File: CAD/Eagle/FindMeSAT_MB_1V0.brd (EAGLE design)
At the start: 99 x 49.2 mm, 127 parts, among them J291 MCX-J-P-X-RA-SM1, J685 SMA_CON, J701 MOLEX_105017-0001, J801 MICROSIM-8P_SDCARD-8P_MOLEX-1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, J901 JST_S3B-XH-A, Q101 ABS07, Q651 ABM3B-16MHZ-10-R50-1-U, U1001 CFPT-141, U101 ATXMEGA256A3BU-AU, U1011 OPA354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

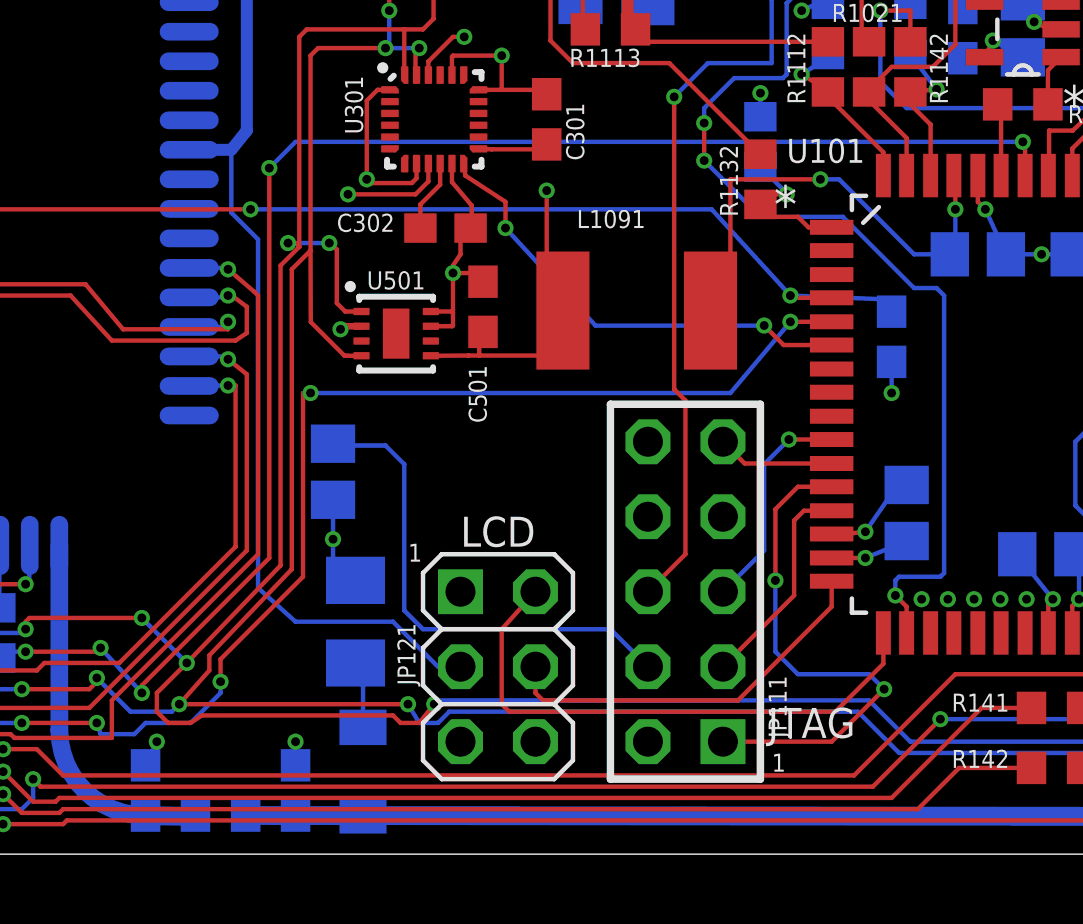
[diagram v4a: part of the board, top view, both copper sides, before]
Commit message: Eagle - I/O header added
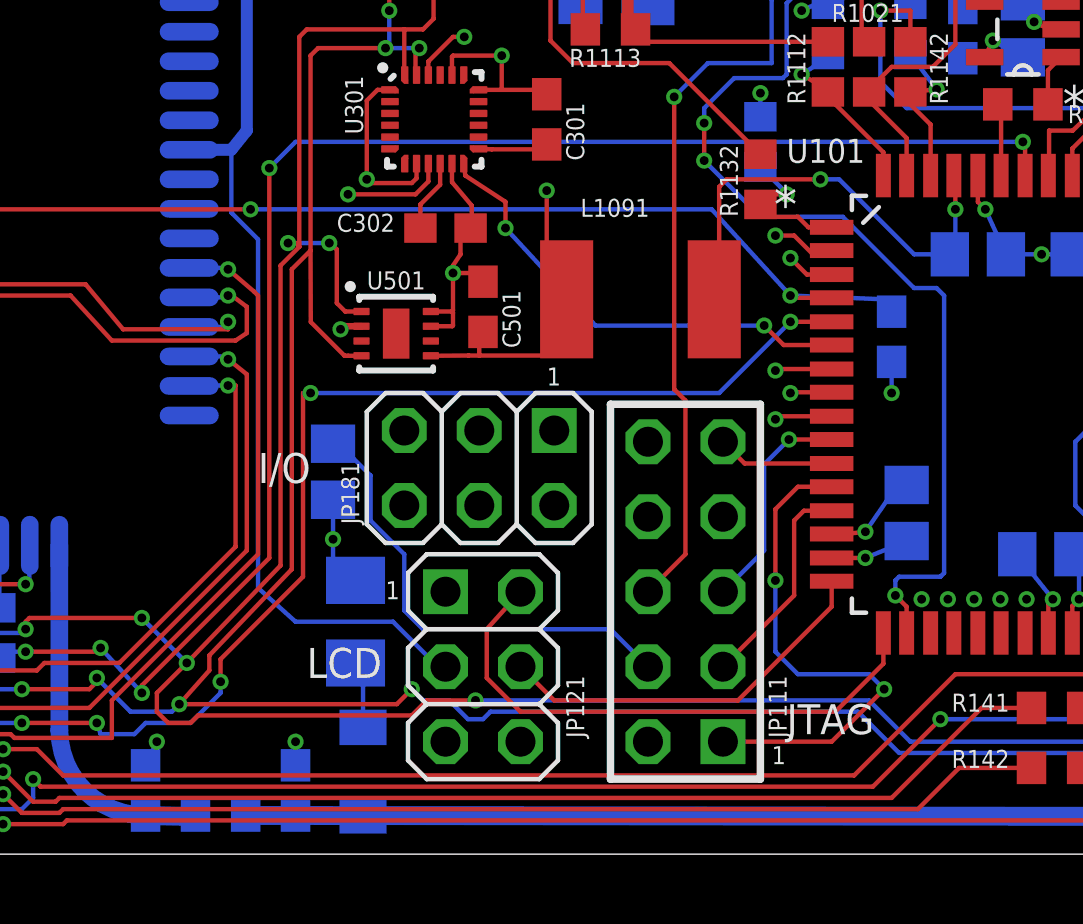
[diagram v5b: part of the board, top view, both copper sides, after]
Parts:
- added JP181: (no value), df4iah_connector:2X03
- moved JP121 0.51 mm to (51.6, 6.35)
- moved L1091 0.40 mm to (56.9, 18.8)
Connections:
- new net IO_AD1: JP181.3, U101.2
- new net IO_AD2: JP181.5, U101.3
- new net IO_D1: JP181.2, U101.7
- new net IO_D2: JP181.4, U101.8
- new net IO_D3: JP181.6, U101.9
- net GND: now also JP181.1
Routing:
- net IO_AD1: track 0.00 -> 25.2 mm, vias 0 -> 1
- net IO_D3: track 0.00 -> 19.1 mm, vias 0 -> 1
- net IO_AD2: track 0.00 -> 17.9 mm, vias 0 -> 1
- net IO_D2: track 0.00 -> 16.3 mm, vias 0 -> 1
- net IO_D1: track 0.00 -> 12.8 mm, vias 0 -> 1
- net VREF: track 16.7 -> 15.8 mm
- net +5V: track 129.0 -> 128.5 mm
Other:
- board text added: "I/O"

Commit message: Eagle - library entries corrected
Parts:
- C1001, C1002, C101, C1012, C1091, C1092, C1093, C1094, C1095, C1096, C1112, C1121, C301, C302, C401, C501, C601, C611, C612, C711: value 100n -> 100nF
- C1011, C141, C201, C251: value 100p -> 100pF
- C1111, C1113, C712: value 47u -> 47uF
- C681: value 68p -> 68pF
- C686: value 18p -> 18pF
- C701: value 1n -> 1nF
- C901: value 100u -> 100uF
- Q101: value ABS07 -> ABS07-32.768KHZ
- R1001, R1011, R1113: value 100k -> 100kR
- R1002, R112: value 10k -> 10kR
- R1012: value 470k -> 470kR
- R1013: value 10 -> 10R
- R1021, R131, R132, R141, R142, R151, R152, R162, R163, R171, R172, R173, R221, R222, R223, R224, R231, R232, R233, R234, R241, R251: value 27 -> 27R
- R111: value 150 -> 150R
- R1111, R1131, R1141: value 4.02k -> 4.02kR
- R1112, R1132: value 6.04k -> 6.04kR
- R1114: value 15k -> 15kR
- R1115: value 68k -> 68kR
- R1142: value 2.0k -> 2.0kR
- R161: value 4.7k -> 4.7kR
- R211, R212: value 3.3k -> 3.3kR
- R701: value 330k -> 330kR
- R721: value 1k5 -> 1.5kR
- R722, R723, R725: value 68 -> 68R
- R724: value 1M -> 1MR
- RPOLY291: value 150mA -> 0A150
- RPOLY711: value 1A -> 1A0
- U1001: value CFPT-141 -> CFPT-141-20MHZ
- U301: value 9DoF IMU -> MPU-9250

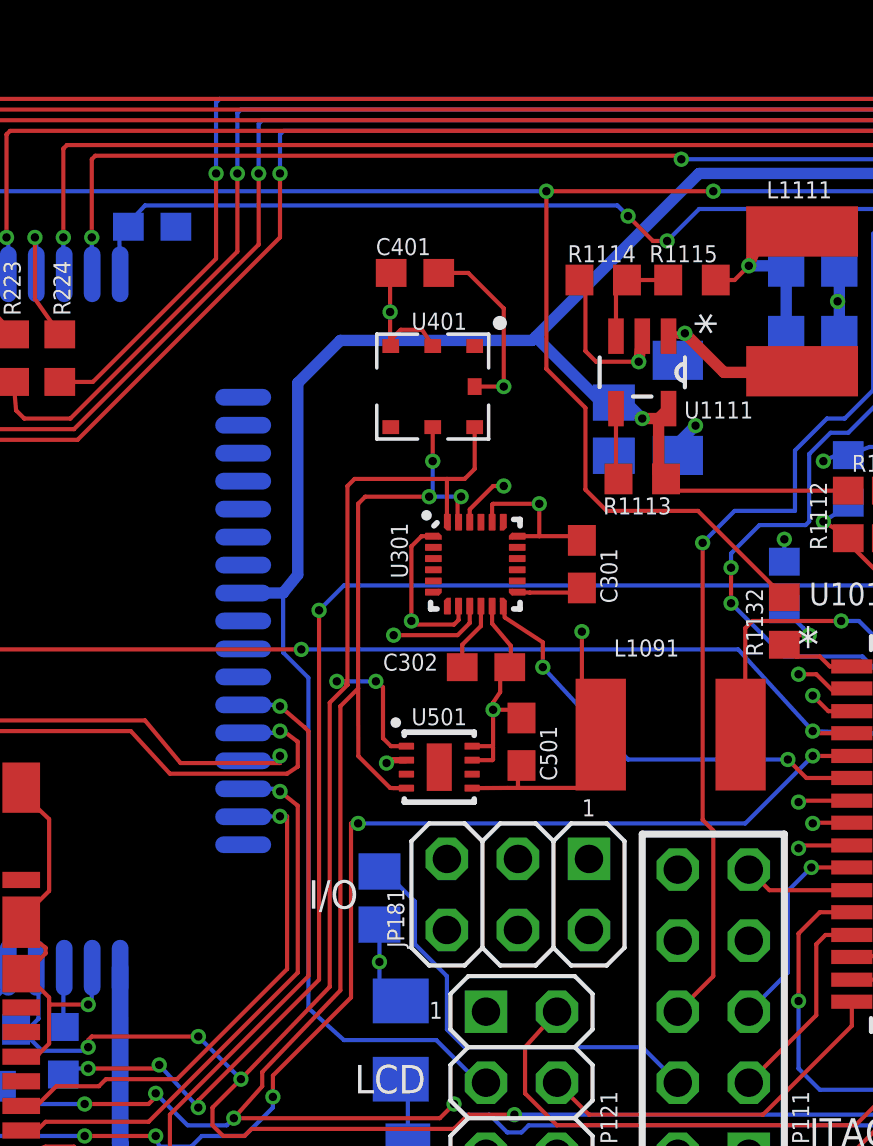
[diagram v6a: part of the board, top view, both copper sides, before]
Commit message: Eagle - new baro device placed
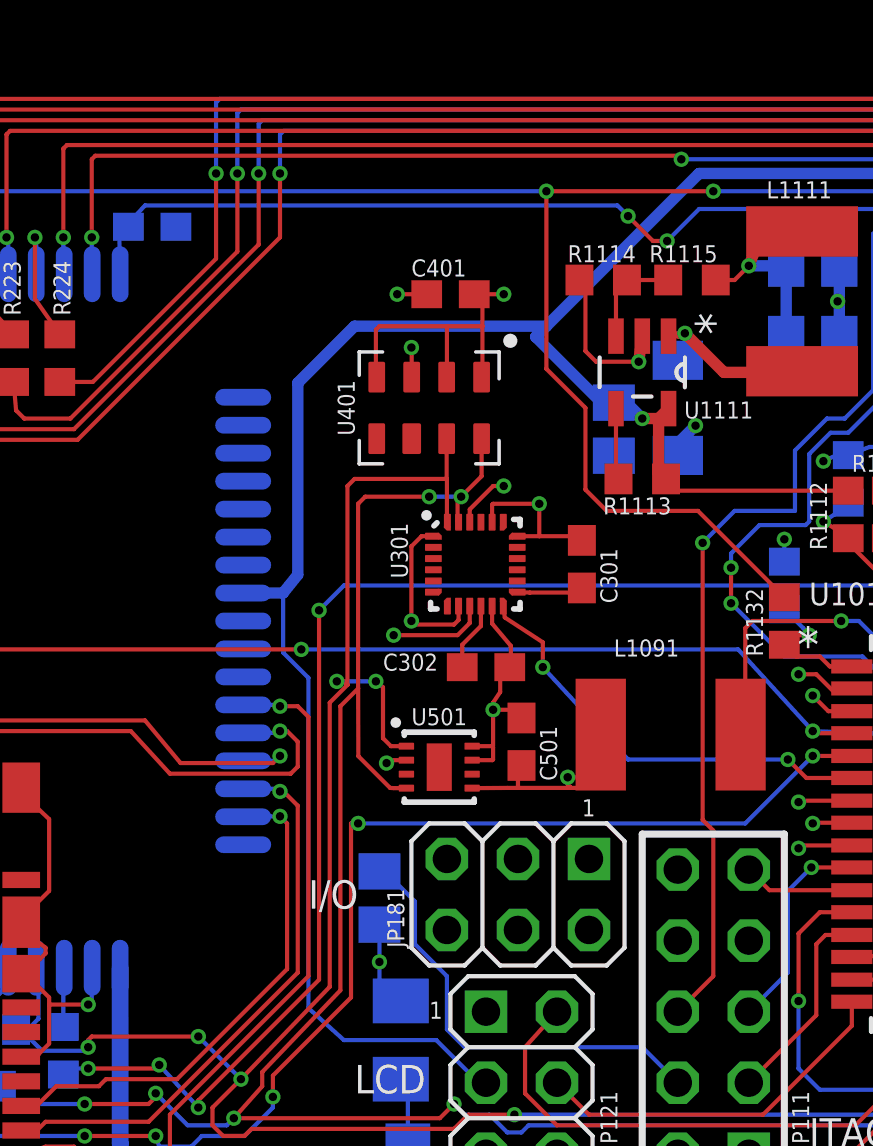
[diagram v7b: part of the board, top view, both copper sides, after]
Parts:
- U401: value BMP180 -> MS5607-02BA03; device df4iah_sensors:BMP180 -> df4iah_sensors:MS5607-02BA
- moved C401 1.48 mm to (49.0, 34.5), turned to 180 degrees
- moved U401 0.77 mm to (48.3, 30.5), turned to 270 degrees
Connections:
- net +3V3: now also U401.1, U401.4; no longer U401.3
- net GND: now also U401.3; no longer U401.7
- net SCL1: now also U401.8; no longer U401.5
- net SDA1: now also U401.7; no longer U401.6
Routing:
- net +3V3: track 62.8 -> 69.9 mm
- net GND: track 206.5 -> 202.0 mm, vias 49 -> 50
- net SDA1: track 97.3 -> 96.1 mm
- net +5V: track 128.5 -> 129.1 mm
- net SCL1: track 99.0 -> 98.9 mm, vias 8 -> 7

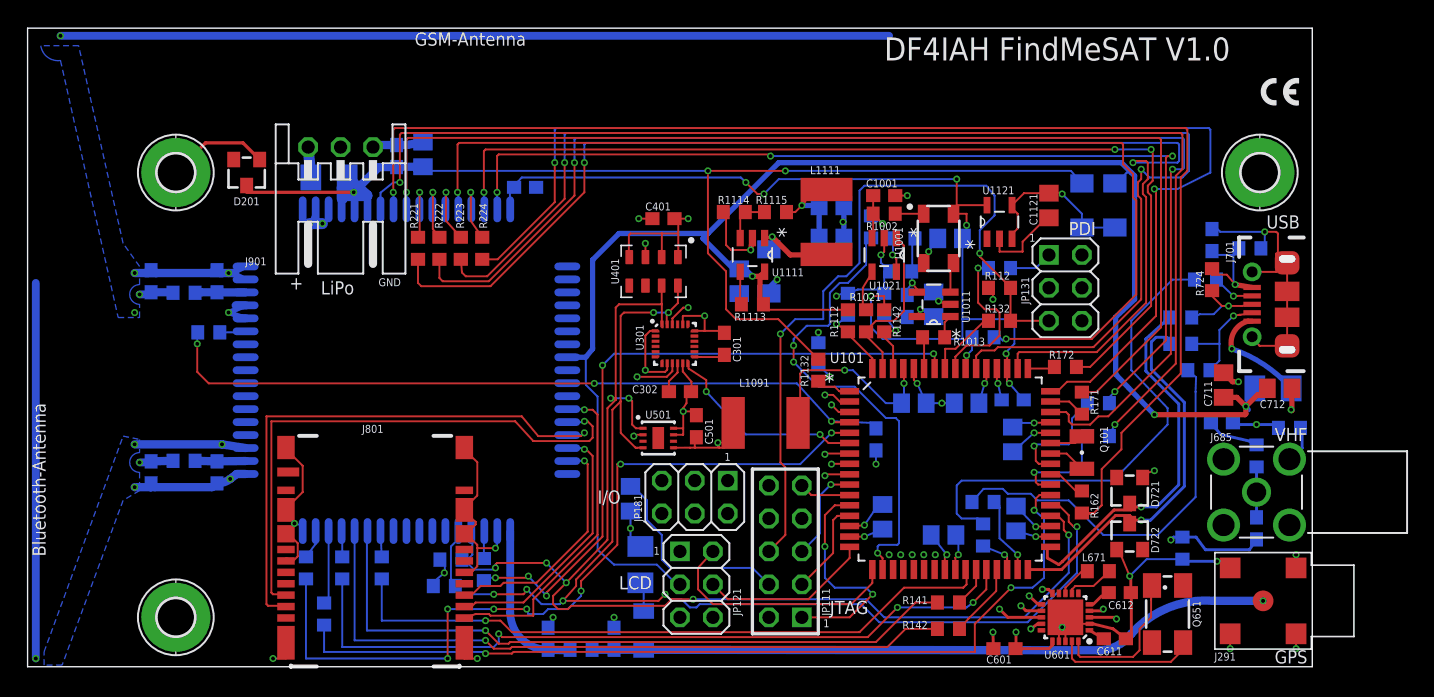
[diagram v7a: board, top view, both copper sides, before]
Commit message: Eagle - minor trimming
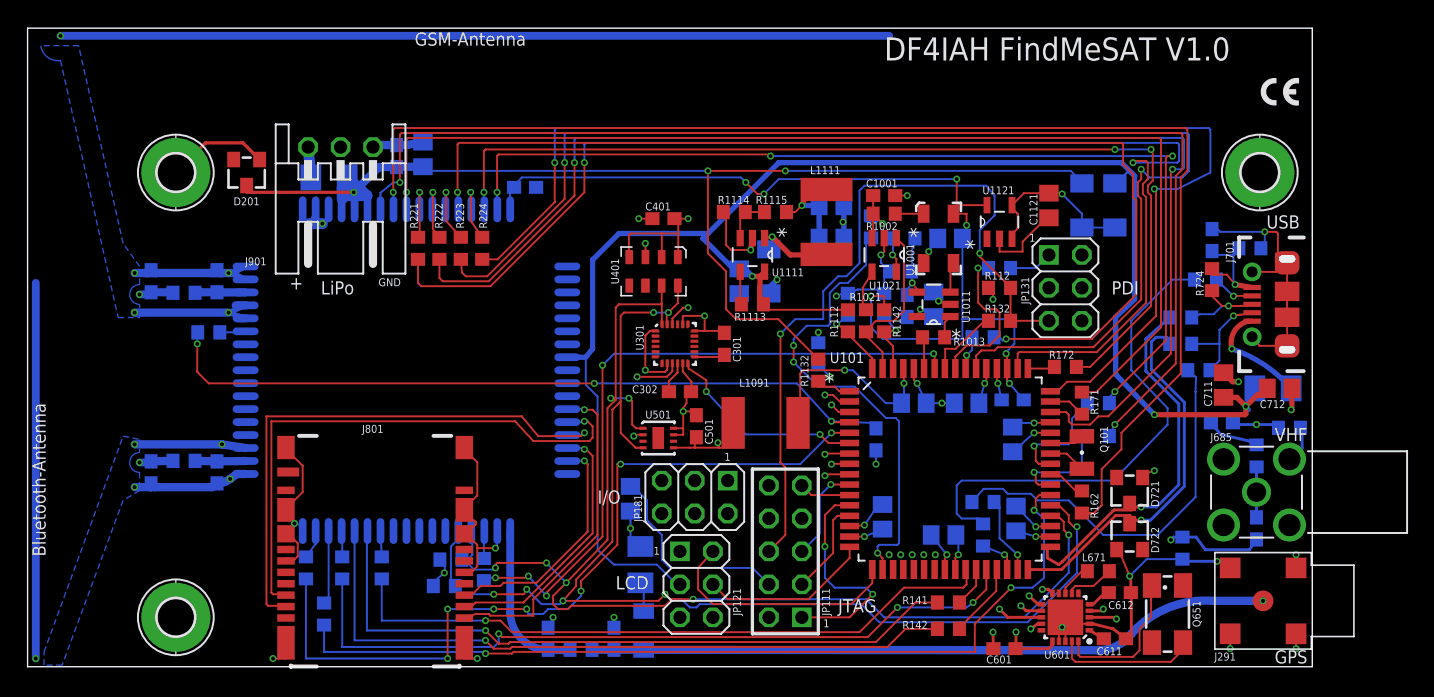
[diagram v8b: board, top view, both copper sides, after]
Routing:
- net GND: track 202.0 -> 209.2 mm
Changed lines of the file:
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@@
 <layer number="43" name="vRestrict" color="2" fill="10" visible="yes" active="yes"/>
 <layer number="44" name="Drills" color="7" fill="1" visible="no" active="yes"/>
-<layer number="45" name="Holes" color="7" fill="1" visible="no" active="yes"/>
+<layer number="45" name="Holes" color="7" fill="1" visible="yes" active="yes"/>
 <layer number="46" name="Milling" color="3" fill="1" visible="yes" active="yes"/>
 <layer number="47" name="Measures" color="7" fill="1" visible="yes" active="yes"/>
-<layer number="48" name="Document" color="7" fill="1" visible="no" active="yes"/>
+<layer number="48" name="Document" color="7" fill="1" visible="yes" active="yes"/>
 <layer number="49" name="Reference" color="7" fill="1" visible="yes" active="yes"/>
 <layer number="50" name="dxf" color="7" fill="1" visible="no" active="no"/>
@@
 <text x="20.193" y="29.083" size="1.016" layer="21" ratio="20">+</text>
 <text x="27.051" y="29.337" size="0.6096" layer="21" ratio="20">GND</text>
-<text x="45.593" y="5.969" size="1.016" layer="21" ratio="20">LCD</text>
-<text x="61.849" y="4.064" size="1.016" layer="21" ratio="20">JTAG</text>
-<text x="80.264" y="33.274" size="1.016" layer="21" ratio="20">PDI</text>
+<text x="45.339" y="5.969" size="1.016" layer="21" ratio="20">LCD</text>
+<text x="62.484" y="4.191" size="1.016" layer="21" ratio="20">JTAG</text>
+<text x="83.566" y="28.702" size="1.016" layer="21" ratio="20">PDI</text>
 <text x="43.942" y="12.573" size="1.016" layer="21" ratio="20">I/O</text>
 <text x="53.721" y="15.875" size="0.6096" layer="21" ratio="20">1</text>
@@
 <attribute name="MPN" value="LFTVXO022175" x="70.231" y="33.02" size="0.6096" layer="27" display="off"/>
 <attribute name="MF" value="IQD-FREQUENCY-PRODUCTS" x="70.231" y="33.02" size="0.6096" layer="27" display="off"/>
-<attribute name="NAME" x="67.470896875" y="31.4258" size="0.6096" layer="25" rot="R90"/>
+<attribute name="NAME" x="68.359896875" y="30.1558" size="0.6096" layer="25" rot="R90"/>
 <attribute name="VALUE" x="72.23333125" y="33.267525" size="0.6096" layer="27" rot="R180"/>
 </element>
@@
 <wire x1="47.117" y1="34.544" x2="48.172" y2="34.544" width="0.15" layer="1"/>
 <wire x1="46.736" y1="17.78" x2="46.736" y2="17.883" width="0.15" layer="1"/>
+<wire x1="8.255" y1="27.305" x2="15.494" y2="27.305" width="0.64" layer="16"/>
 <wire x1="70.17" y1="33.02" x2="74.93" y2="32.9946" width="0" layer="19" extent="1-16"/>
 <wire x1="33.672" y1="10.25" x2="34.163" y2="9.906" width="0" layer="19" extent="1-1"/>
